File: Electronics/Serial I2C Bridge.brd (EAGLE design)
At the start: 41.6 x 44.4 mm, 22 parts, among them IC1 ATmega328P, Q1 16MHz

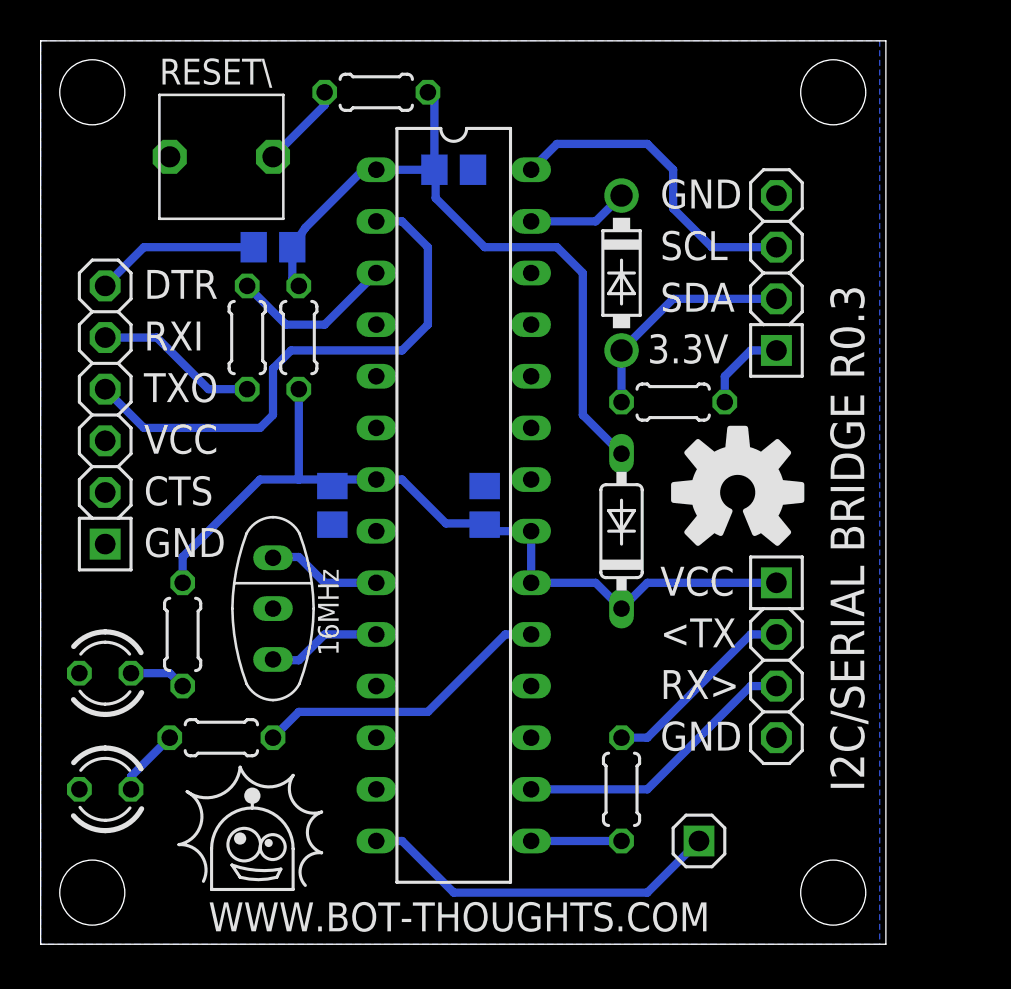
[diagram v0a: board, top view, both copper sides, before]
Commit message: Revised level shift circuit
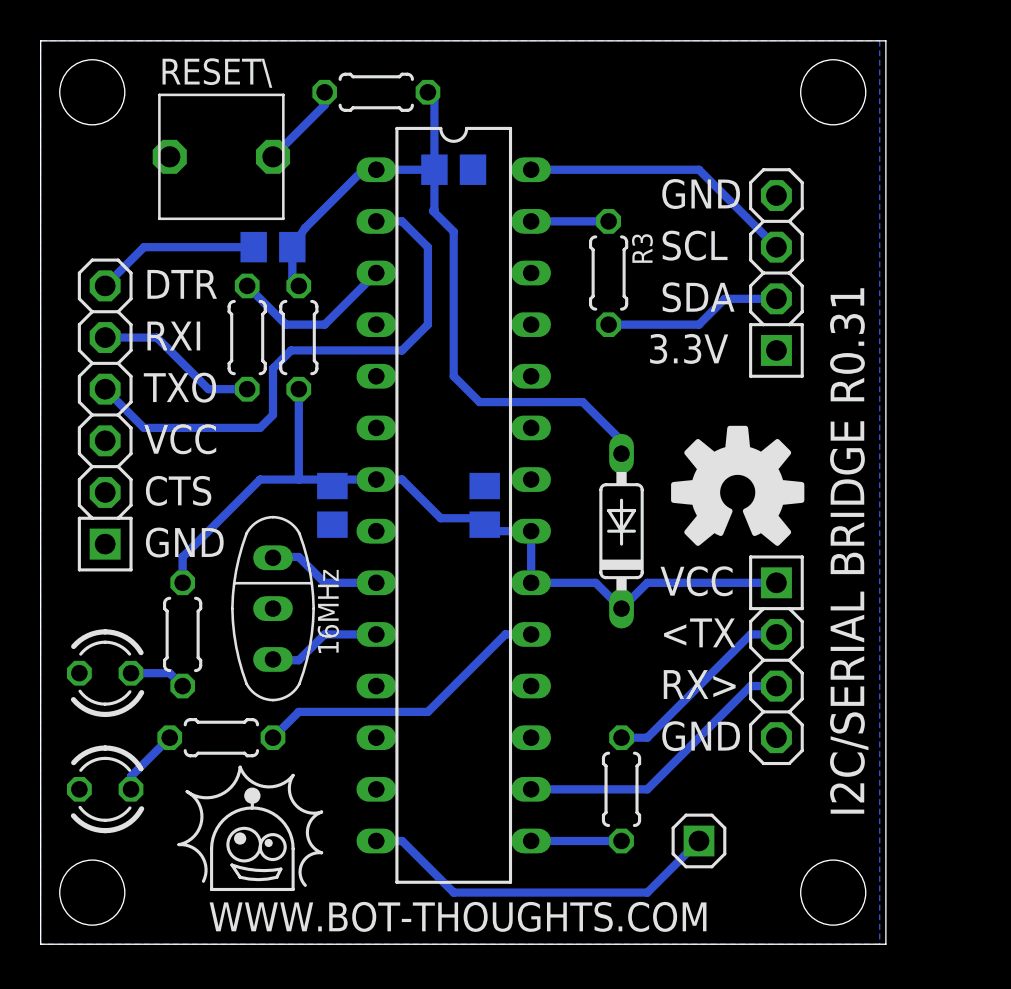
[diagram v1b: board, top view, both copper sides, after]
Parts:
- removed D1: 1N5817, diode:DO41-7.6
- R3: value 2.2k -> 1K
- moved R3 7.10 mm to (27.9, 33.0), turned to 270 degrees
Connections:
- net VCC renamed 5V
- net 3.3V: no longer R3.2
- net LV_SDA: now also R3.2; no longer D1.A, R3.1
- net SDA: now also R3.1; no longer D1.C
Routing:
- net 3.3V: track 4.34 -> 0.00 mm
- net LV_SDA: track 11.2 -> 8.78 mm
- net SCL: track 15.8 -> 13.6 mm
- net SDA: track 4.97 -> 3.81 mm
- net N$6: track 34.5 -> 35.5 mm
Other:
- board text added: "I2C/SERIAL BRIDGE R0.31"
- board text removed: "I2C/SERIAL BRIDGE R0.3"

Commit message: Moved RC Mux to subdirectory. Minor changes to various other boards.
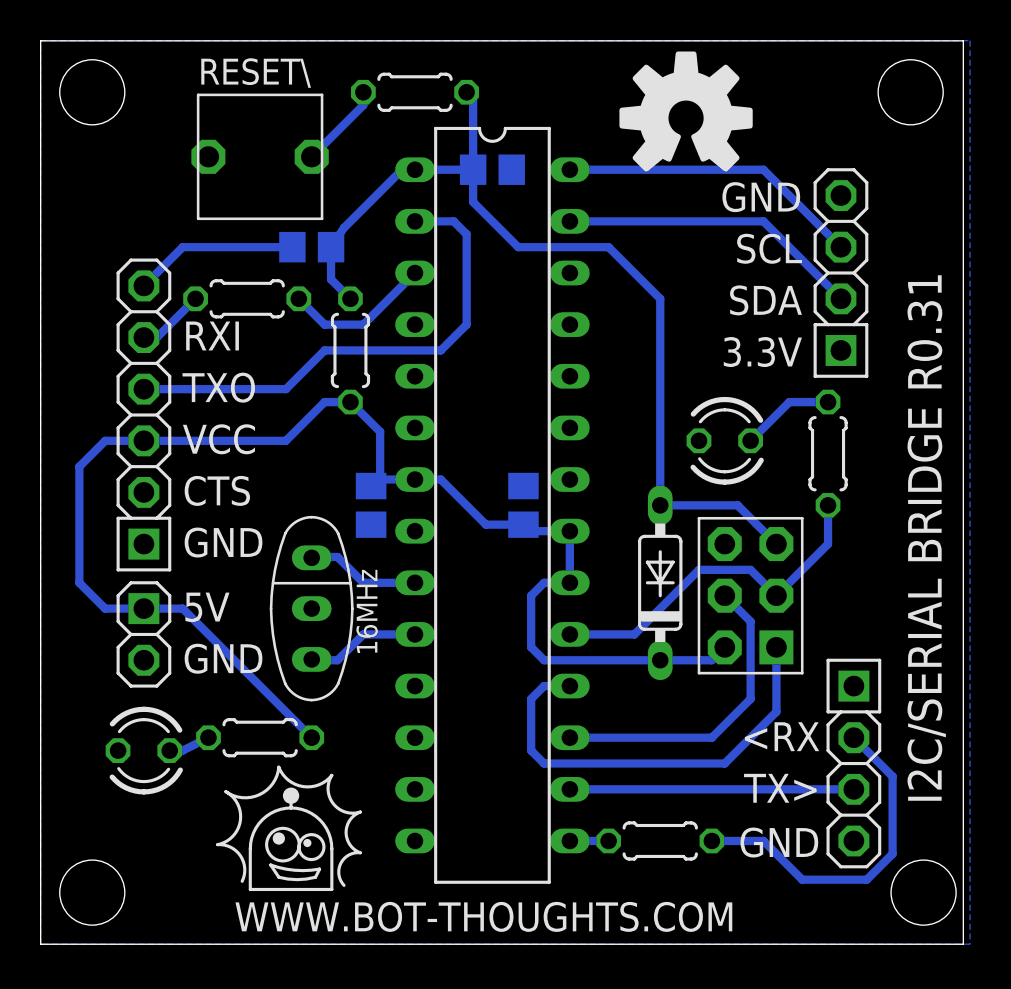
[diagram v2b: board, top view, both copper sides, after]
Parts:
- removed JP3: RDY, pinhead-2:1X01-S
- removed R3: 1K, rcl:0204/5
- added J1: AVRISP, ads4:CON6P2R
- added JP5: PWR, pinhead-2:1X02-S
- JP2: value CAM -> DIAG
- moved LED1 35.0 mm to (33.7, 24.8)
- moved R2 33.0 mm to (38.7, 24.1), turned to 90 degrees
- moved JP2 6.35 mm to (40.0, 8.89)
- moved R7 6.35 mm to (10.8, 10.2), turned to 180 degrees
- moved LED2 4.26 mm to (5.08, 9.53)
- moved R4 3.18 mm to (30.5, 5.08), turned to 0 degrees
- moved D2 3.18 mm to (30.5, 17.8)
- moved JP1 3.17 mm to (39.4, 33.0)
- moved R1 2.62 mm to (15.2, 29.2)
- moved C1 1.91 mm to (13.3, 34.3)
- moved C2 1.91 mm to (22.2, 38.1)
- moved IC1 1.91 mm to (22.2, 21.6)
- moved Q1 1.91 mm to (13.3, 16.5)
- moved R6 1.91 mm to (10.2, 31.8), turned to 180 degrees
- moved S1 1.91 mm to (8.26, 38.7)
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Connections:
- removed net LV_SDA: JP1.2, R3.2
- removed net N$5: IC1.19, R2.1
- removed net N$6: C1.1, C2.1, D2.A, IC1.1, R1.1, R5.1
- removed net READY: IC1.14, JP3.1
- new net !RESET: C1.1, C2.1, D2.A, IC1.1, J1.5, R1.1, R5.1
- new net MISO: IC1.18, J1.1
- new net MOSI: IC1.17, J1.4
- new net SCK: IC1.19, J1.3, R2.1
- net 5V: now also J1.2, JP4.3, JP5.1; no longer JP2.1
- net GND: now also J1.6, JP5.2
- net SDA: now also JP1.2; no longer R3.1
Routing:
- net !RESET: track 0.00 -> 45.0 mm
- net N$6: track 35.5 -> 0.00 mm
- net 5V: track 42.1 -> 67.6 mm
- net MISO: track 0.00 -> 21.3 mm
- net READY: track 18.0 -> 0.00 mm
- net SCK: track 0.00 -> 17.5 mm
- net MOSI: track 0.00 -> 15.3 mm
- net N$5: track 14.8 -> 0.00 mm
- net SDA: track 3.81 -> 14.9 mm
- net LV_SDA: track 8.78 -> 0.00 mm
- net LV_TX>: track 9.72 -> 16.7 mm
- net LV_TXD/RXI>: track 8.04 -> 3.33 mm
- net <RXD/TXO: track 27.0 -> 24.4 mm
- net TX>: track 4.45 -> 1.91 mm
- net N$4: track 3.33 -> 4.60 mm
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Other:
- board size 41.6 x 44.4 mm -> 45.4 x 44.4 mm
- board text added: "5V"
- board text added: "<RX"
- board text added: "TX>"
- board text removed: "<TX"
- board text removed: "DTR"
- board text removed: "RX>"
